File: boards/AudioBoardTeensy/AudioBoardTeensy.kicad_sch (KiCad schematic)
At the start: 11 parts, among them J1 54-00174, J3 Conn_01x20_Pin, U1 Teensy4.0

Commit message: Fix audio board flipped audio jack pins
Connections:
- net AUDIO: now also J1.2; no longer J1.1
- net GND: now also J1.1; no longer J1.2
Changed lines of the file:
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@@
+		)
+	)
+	(global_label "MOSI"
+		(shape output)
+		(at 201.93 80.01 180)
+		(fields_autoplaced yes)
+		(effects
+			(font
+				(size 1.27 1.27)
+			)
+			(justify right)
+		)
+		(property "Intersheetrefs" "${INTERSHEET_REFS}"
+			(at 194.3486 80.01 0)
+			(effects
+				(font
+					(size 1.27 1.27)
+				)
+				(justify right)
+				(hide yes)
+			)
+		)
+	)
+	(global_label "A0"
+		(shape output)
+		(at 201.93 100.33 180)
+		(fields_autoplaced yes)
+		(effects
+			(font
+				(size 1.27 1.27)
+			)
+			(justify right)
+		)
+		(property "Intersheetrefs" "${INTERSHEET_REFS}"
+			(at 196.6467 100.33 0)
+			(effects
+				(font
+					(size 1.27 1.27)
+				)
+				(justify right)
+				(hide yes)
+			)
 		)
 	)
 	(global_label "AUDIO"
 		(shape output)
-		(at 41.91 54.61 0)
+		(at 40.64 64.77 0)
 		(fields_autoplaced yes)
 		(effects
@@
 		)
 		(property "Intersheetrefs" "${INTERSHEET_REFS}"
-			(at 50.5196 54.61 0)
+			(at 49.2496 64.77 0)
 			(effects
 				(font
@@
 				)
 				(justify left)
-				(hide yes)
-			)
-		)
-	)
-	(global_label "MOSI"
-		(shape output)
-		(at 201.93 80.01 180)
-		(fields_autoplaced yes)
-		(effects
-			(font
-				(size 1.27 1.27)
-			)
-			(justify right)
-		)
-		(property "Intersheetrefs" "${INTERSHEET_REFS}"
-			(at 194.3486 80.01 0)
-			(effects
-				(font
-					(size 1.27 1.27)
-				)
-				(justify right)
-				(hide yes)
-			)
-		)
-	)
-	(global_label "A0"
-		(shape output)
-		(at 201.93 100.33 180)
-		(fields_autoplaced yes)
-		(effects
-			(font
-				(size 1.27 1.27)
-			)
-			(justify right)
-		)
-		(property "Intersheetrefs" "${INTERSHEET_REFS}"
-			(at 196.6467 100.33 0)
-			(effects
-				(font
-					(size 1.27 1.27)
-				)
-				(justify right)
 				(hide yes)
 			)
@@
 	(symbol
 		(lib_id "power:GND")
-		(at 40.64 64.77 90)
+		(at 41.91 54.61 90)
 		(unit 1)
 		(exclude_from_sim no)
@@
 		(fields_autoplaced yes)
 		(property "Reference" "#PWR01"
-			(at 46.99 64.77 0)
+			(at 48.26 54.61 0)
 			(effects
 				(font
@@
 		)
 		(property "Value" "GND"
-			(at 44.45 64.7699 90)
+			(at 45.72 54.6099 90)
 			(effects
 				(font
@@
 		)
 		(property "Footprint" ""
-			(at 40.64 64.77 0)
+			(at 41.91 54.61 0)
 			(effects
 				(font
@@
 		)
 		(property "Datasheet" ""
-			(at 40.64 64.77 0)
+			(at 41.91 54.61 0)
 			(effects
 				(font
@@
 		)
 		(property "Description" "Power symbol creates a global label with name \"GND\" , ground"
-			(at 40.64 64.77 0)
+			(at 41.91 54.61 0)
 			(effects
 				(font
@@
 		)
 		(instances
-			(project ""
+			(project "AudioBoardTeensy"
 				(path "/eab36e20-2eac-4566-809f-58ea7d09a296"
 					(reference "#PWR01")

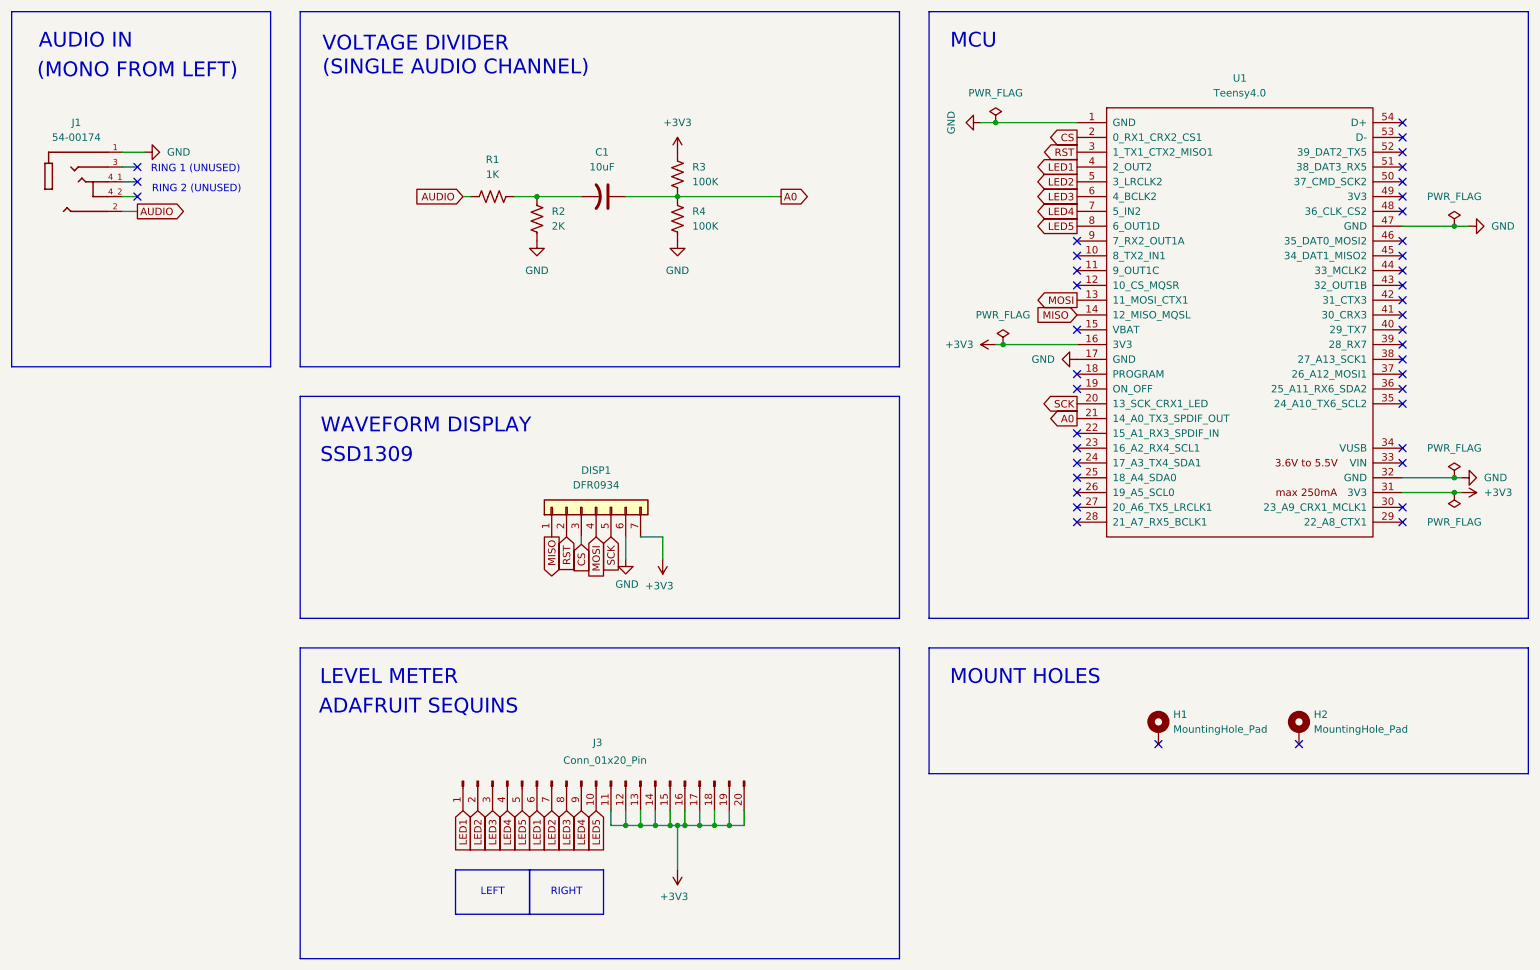
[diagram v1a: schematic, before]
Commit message: Re-route audio board
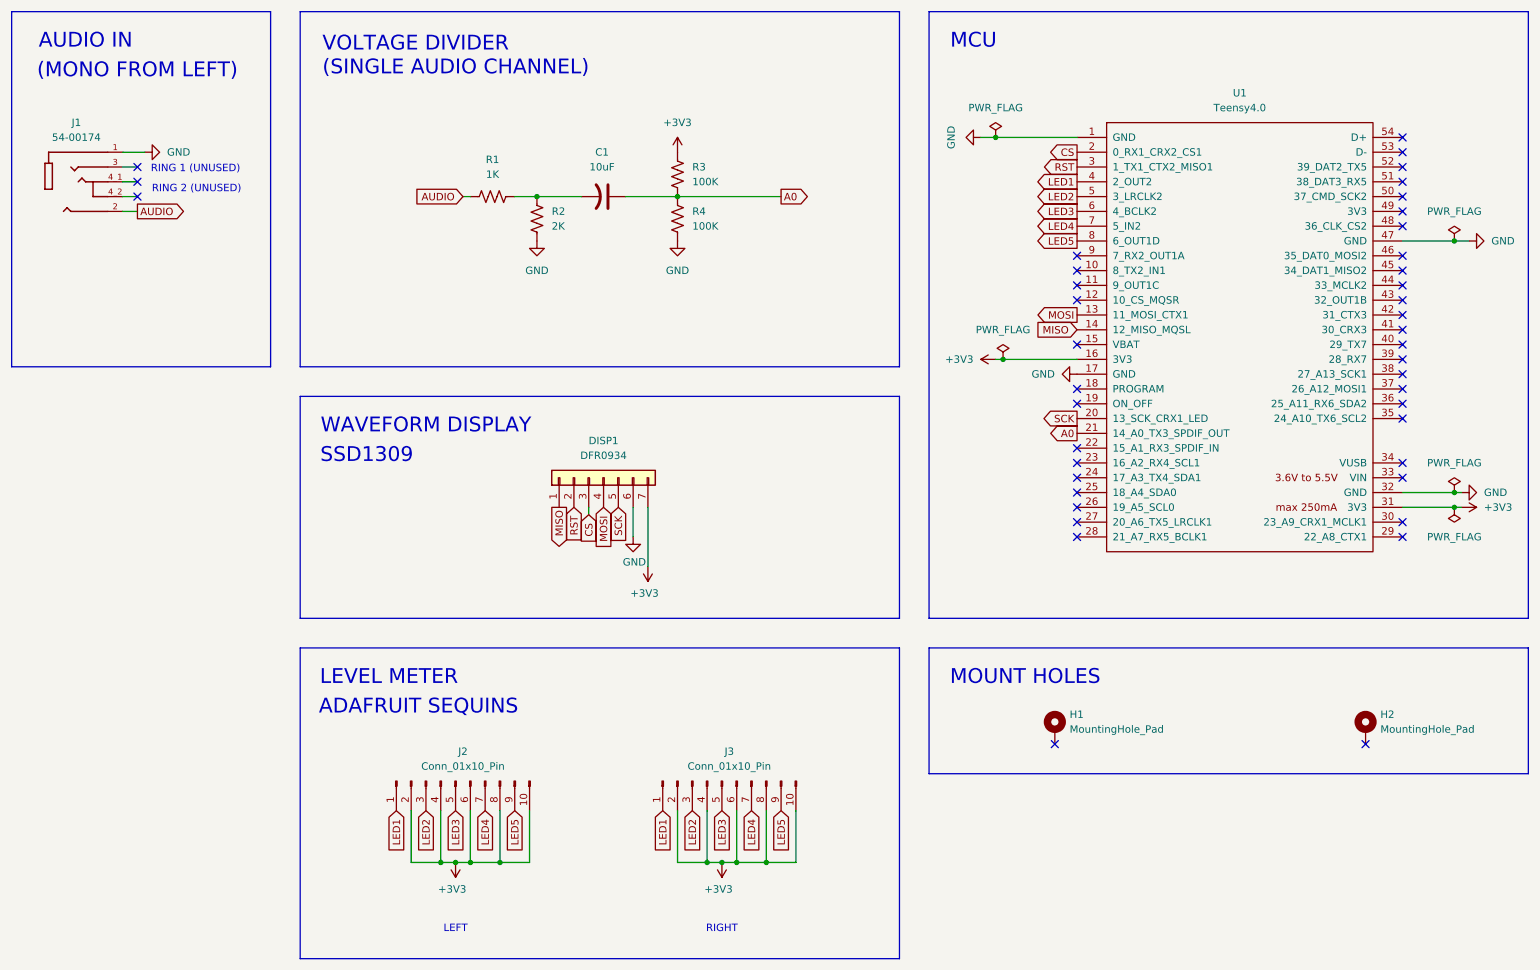
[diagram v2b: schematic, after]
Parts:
- removed J3: Conn_01x20_Pin, Connector_PinHeader_2.54mm:PinHeader_1x20_P2.54mm_Vertical, symbol Connector:Conn_01x20_Pin
- added J2, J3: Conn_01x10_Pin, Connector_PinHeader_2.54mm:PinHeader_1x10_P2.54mm_Vertical, symbol Connector:Conn_01x10_Pin
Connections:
- net +3V3: now also J2.10 (Pin_10), J2.2 (Pin_2), J2.4 (Pin_4), J2.6 (Pin_6), J2.8 (Pin_8), J3.10 (Pin_10), J3.2 (Pin_2), J3.4 (Pin_4), J3.6 (Pin_6), J3.8 (Pin_8)
- net LED1: now also J2.1 (Pin_1), J3.1 (Pin_1)
- net LED2: now also J2.3 (Pin_3), J3.3 (Pin_3)
- net LED3: now also J2.5 (Pin_5), J3.5 (Pin_5)
- net LED4: now also J2.7 (Pin_7), J3.7 (Pin_7)
- net LED5: now also J2.9 (Pin_9), J3.9 (Pin_9)
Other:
- moved on the sheet: DISP1, H1, H2, U1

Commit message: Another iteration of boards
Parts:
- renumbered DISP1 to J4
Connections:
- net AUDIO: now also J1.4_1; no longer J1.2
- net GND: now also J1.2
- net RING 1: now reaches J1.3
- net TIP 2: now reaches J1.4_2
- no-connect marks 42 -> 41
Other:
- note added: "AUDIO LEVEL METER"
- note added: "AUDIO SIGNAL VOLTAGE DIVIDER (SINGLE AUDIO CHANNEL)"
- note added: "AUDIO WAVEFORM DISPLAY"
- note added: "TRRS"
- note removed: "(MONO FROM LEFT)"
- note removed: "LEVEL METER"
- note removed: "RING 1 (UNUSED)"
- note removed: "RING 2 (UNUSED)"
- note removed: "VOLTAGE DIVIDER (SINGLE AUDIO CHANNEL)"
- note removed: "WAVEFORM DISPLAY"
- moved on the sheet: J1, J4

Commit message: Re-finalize audio board and cleanup
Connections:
- net RING 1 is gone; now on net GND: J1.3
- net +3V3: now also J2.7 (Pin_7), J2.9 (Pin_9), J3.7 (Pin_7), J3.9 (Pin_9); no longer J2.2 (Pin_2), J2.4 (Pin_4), J3.2 (Pin_2), J3.4 (Pin_4)
- net AUDIO: now also J1.2; no longer J1.4_1
- net GND: no longer J1.2
- net LED2: now also J2.2 (Pin_2), J3.2 (Pin_2); no longer J2.3 (Pin_3), J3.3 (Pin_3)
- net LED3: now also J2.3 (Pin_3), J3.3 (Pin_3); no longer J2.5 (Pin_5), J3.5 (Pin_5)
- net LED4: now also J2.4 (Pin_4), J3.4 (Pin_4); no longer J2.7 (Pin_7), J3.7 (Pin_7)
- net LED5: now also J2.5 (Pin_5), J3.5 (Pin_5); no longer J2.9 (Pin_9), J3.9 (Pin_9)
- new net TIP 1: J1.4_1
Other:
- moved on the sheet: J1
